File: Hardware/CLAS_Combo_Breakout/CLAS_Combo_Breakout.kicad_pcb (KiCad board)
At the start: 4 copper layers, 60 x 60 mm, 89 parts, among them J1 USB_C_Receptacle_USB2.0, J2 ZED, J3 NEO, J4 USB_C_Receptacle_USB2.0, J5 Conn_SMA, U1 USBLC6-2P6, U10 NT1191GEAE3S, U2 ZED-F9P, U3 NEO-D9C-00B, U4 USBLC6-2P6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

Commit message: 配線中
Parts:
- removed C9: 0.1u, Capacitor_SMD:C_0603_1608Metric
- moved C8 0.80 mm to (158.2, 130.1), turned to -90 degrees
- moved U6 0.76 mm to (157.9, 125.8)
- moved R4 0.57 mm to (153.1, 134.2)
- moved R18 0.57 mm to (155.9, 134.2)
- moved R3 0.36 mm to (153.1, 132.9)
- moved R27 0.36 mm to (155.9, 132.9)
- moved BT1 0.25 mm to (154.4, 129.6)
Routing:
- net /EXTINT_ZED: track 0.00 -> 25.3 mm, vias 0 -> 1
- net /TP: track 6.16 -> 29.6 mm, vias 0 -> 2
- net Net-(TP1-Pad1): track 0.00 -> 20.3 mm, vias 0 -> 2
- net /TX_RDY_: track 0.00 -> 15.0 mm, vias 0 -> 2
- net /RXD1_ZED: track 1.34 -> 14.7 mm
- net /VBUS_ZED: track 5.00 -> 11.0 mm, vias 2 -> 3

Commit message: 配線中
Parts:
- moved D7 3.30 mm to (158.2, 130.4), turned to 90 degrees
- moved R3 2.59 mm to (155.6, 133.4)
- moved R27 2.50 mm to (158.2, 133.9), turned to -90 degrees
- moved C8 1.91 mm to (158.2, 128.2), turned to 0 degrees
- moved R18 0.51 mm to (155.9, 134.7)
- moved R4 0.51 mm to (153.1, 134.7)
- moved BT1 0.25 mm to (154.4, 129.9)
- moved U6 0.25 mm to (157.9, 125.6)
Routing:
- net /V_BACKUP: track 0.00 -> 22.4 mm, vias 0 -> 2
- net /SDA: track 17.8 -> 32.9 mm, vias 0 -> 1
- net /SCL: track 12.7 -> 27.3 mm
- net /VBUS_ZED: track 11.0 -> 23.4 mm, vias 3 -> 4
- net /VBUS_NEO: track 29.3 -> 41.6 mm, vias 3 -> 4
- net +5V: track 0.00 -> 7.06 mm
- net /SCL_ZED_: track 0.00 -> 6.95 mm
- net /CC2_ZED: track 0.00 -> 5.75 mm
- net /SDA_ZED_: track 0.00 -> 4.21 mm
- net +3.3V: track 81.7 -> 85.9 mm
- net Net-(D7-Pad1): track 0.00 -> 1.78 mm

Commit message: I2C系統を配線
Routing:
- net /SDA: track 32.9 -> 82.6 mm
- net /SCL: track 27.3 -> 74.1 mm, vias 0 -> 1
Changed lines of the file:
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@@
   (via (at 151.562 101.316) (size 0.6) (drill 0.3) (layers "F.Cu" "B.Cu") (net 11))
   (arc (start 151.93 106.116) (mid 151.669785 106.008215) (end 151.562 105.748) (width 0.3) (layer "F.Cu") (net 11))
-  (segment (start 153.848 104.986) (end 151.562 104.986) (width 0.3) (layer "B.Cu") (net 11))
-  (segment (start 155.372 106.51) (end 153.848 104.986) (width 0.3) (layer "B.Cu") (net 11))
+  (segment (start 153.594 104.986) (end 151.562 104.986) (width 0.3) (layer "B.Cu") (net 11))
+  (segment (start 155.372 123.782) (end 155.372 109.304) (width 0.3) (layer "B.Cu") (net 11))
   (segment (start 154.356 96.604) (end 155.626 96.604) (width 0.3) (layer "B.Cu") (net 11))
+  (segment (start 154.864 108.796) (end 154.864 106.256) (width 0.3) (layer "B.Cu") (net 11))
   (segment (start 151.562 101.316) (end 151.562 99.398) (width 0.3) (layer "B.Cu") (net 11))
-  (segment (start 155.372 123.782) (end 155.372 106.51) (width 0.3) (layer "B.Cu") (net 11))
+  (segment (start 155.372 109.304) (end 154.864 108.796) (width 0.3) (layer "B.Cu") (net 11))
+  (segment (start 154.864 106.256) (end 153.594 104.986) (width 0.3) (layer "B.Cu") (net 11))
   (arc (start 151.562 99.398) (mid 152.380344 97.422344) (end 154.356 96.604) (width 0.3) (layer "B.Cu") (net 11))
   (segment (start 146.101 109.685) (end 142.829815 109.685) (width 0.35) (layer "F.Cu") (net 12))
@@
   (segment (start 150.546 145.88) (end 151.753 145.88) (width 0.2) (layer "F.Cu") (net 25))
   (segment (start 128.322 120.988) (end 126.866 120.988) (width 0.25) (layer "F.Cu") (net 27))
-  (segment (start 155.372 144.864) (end 154.356 145.88) (width 0.2) (layer "F.Cu") (net 28))
-  (segment (start 156.388 141.308) (end 155.372 142.324) (width 0.2) (layer "F.Cu") (net 28))
+  (segment (start 154.356 145.88) (end 153.403 145.88) (width 0.2) (layer "F.Cu") (net 28))
   (segment (start 149.53 92.794) (end 149.53 92.032) (width 0.2) (layer "F.Cu") (net 28))
-  (segment (start 155.88 136.482) (end 156.388 136.99) (width 0.2) (layer "F.Cu") (net 28))
-  (segment (start 154.356 145.88) (end 153.403 145.88) (width 0.2) (layer "F.Cu") (net 28))
-  (segment (start 156.405745 133.543255) (end 156.134 133.815) (width 0.2) (layer "F.Cu") (net 28))
-  (segment (start 156.388 136.99) (end 156.388 141.308) (width 0.2) (layer "F.Cu") (net 28))
+  (segment (start 155.88 134.42821) (end 155.88 135.466) (width 0.2) (layer "F.Cu") (net 28))
   (segment (start 153.34 92.032) (end 152.42921 91.12121) (width 0.2) (layer "F.Cu") (net 28))
   (segment (start 153.34 147.912) (end 153.34 145.943) (width 0.2) (layer "F.Cu") (net 28))
   (segment (start 151.562 90.762) (end 150.8 90.762) (width 0.2) (layer "F.Cu") (net 28))
+  (segment (start 155.372 144.864) (end 154.356 145.88) (width 0.2) (layer "F.Cu") (net 28))
+  (segment (start 155.88 135.466) (end 155.88 136.736) (width 0.2) (layer "F.Cu") (net 28))
+  (segment (start 156.388 137.244) (end 156.388 141.308) (width 0.2) (layer "F.Cu") (net 28))
   (segment (start 155.372 142.324) (end 155.372 144.864) (width 0.2) (layer "F.Cu") (net 28))
   (segment (start 145.148 93.81) (end 148.514 93.81) (width 0.2) (layer "F.Cu") (net 28))
-  (segment (start 155.88 134.42821) (end 155.88 136.482) (width 0.2) (layer "F.Cu") (net 28))
+  (segment (start 156.388 141.308) (end 155.372 142.324) (width 0.2) (layer "F.Cu") (net 28))
+  (segment (start 155.88 136.736) (end 156.388 137.244) (width 0.2) (layer "F.Cu") (net 28))
+  (segment (start 156.134 133.815) (end 156.405745 133.543255) (width 0.2) (layer "F.Cu") (net 28))
+  (via (at 155.88 135.466) (size 0.6) (drill 0.3) (layers "F.Cu" "B.Cu") (net 28))
   (arc (start 149.53 92.032) (mid 149.901974 91.133974) (end 150.8 90.762) (width 0.2) (layer "F.Cu") (net 28))
+  (arc (start 156.405745 133.543255) (mid 156.439239 133.493128) (end 156.451 133.434) (width 0.2) (layer "F.Cu") (net 28))
   (arc (start 148.514 93.81) (mid 149.23242 93.51242) (end 149.53 92.794) (width 0.2) (layer "F.Cu") (net 28))
   (arc (start 152.42921 91.12121) (mid 152.031331 90.855356) (end 151.562 90.762) (width 0.2) (layer "F.Cu") (net 28))
-  (arc (start 156.451 133.434) (mid 156.439239 133.493128) (end 156.405745 133.543255) (width 0.2) (layer "F.Cu") (net 28))
+  (arc (start 155.88 134.42821) (mid 155.946012 134.096343) (end 156.134 133.815) (width 0.2) (layer "F.Cu") (net 28))
   (arc (start 153.34 145.943) (mid 153.358452 145.898452) (end 153.403 145.88) (width 0.2) (layer "F.Cu") (net 28))
-  (arc (start 156.134 133.815) (mid 155.946012 134.096343) (end 155.88 134.42821) (width 0.2) (layer "F.Cu") (net 28))
+  (segment (start 158.674 108.542) (end 158.674 98.636) (width 0.2) (layer "B.Cu") (net 28))
+  (segment (start 153.34 92.94279) (end 153.34 92.032) (width 0.2) (layer "B.Cu") (net 28))
+  (segment (start 157.404 133.942) (end 157.404 121.496) (width 0.2) (layer "B.Cu") (net 28))
+  (segment (start 157.404 121.496) (end 158.42 120.48) (width 0.2) (layer "B.Cu") (net 28))
+  (segment (start 155.88 135.466) (end 157.404 133.942) (width 0.2) (layer "B.Cu") (net 28))
+  (segment (start 158.42 108.796) (end 158.674 108.542) (width 0.2) (layer "B.Cu") (net 28))
+  (segment (start 158.674 98.636) (end 153.594 93.556) (width 0.2) (layer "B.Cu") (net 28))
+  (segment (start 158.42 120.48) (end 158.42 108.796) (width 0.2) (layer "B.Cu") (net 28))
+  (arc (start 153.594 93.556) (mid 153.406013 93.274656) (end 153.34 92.94279) (width 0.2) (layer "B.Cu") (net 28))
   (segment (start 154.61 136.736) (end 154.61 135.466) (width 0.2) (layer "F.Cu") (net 29))
   (segment (start 145.657 145.88) (end 144.853759 146.683241) (width 0.2) (layer "F.Cu") (net 29))
@@
   (arc (start 144.45 147.912) (mid 144.821974 148.810026) (end 145.72 149.182) (width 0.2) (layer "F.Cu") (net 29))
   (arc (start 146.736 95.08) (mid 146.970665 95.033322) (end 147.169605 94.900395) (width 0.2) (layer "F.Cu") (net 29))
+  (segment (start 154.102 102.446) (end 156.134 104.478) (width 0.2) (layer "B.Cu") (net 29))
   (segment (start 150.8 144.61) (end 150.8 147.912) (width 0.2) (layer "B.Cu") (net 29))
+  (segment (start 150.8 92.032) (end 150.8 101.684) (width 0.2) (layer "B.Cu") (net 29))
+  (segment (start 156.388 125.56) (end 154.61 127.338) (width 0.2) (layer "B.Cu") (net 29))
+  (segment (start 156.134 104.478) (end 156.134 108.542) (width 0.2) (layer "B.Cu") (net 29))
   (segment (start 154.61 140.8) (end 150.8 144.61) (width 0.2) (layer "B.Cu") (net 29))
   (segment (start 154.61 136.736) (end 154.61 140.8) (width 0.2) (layer "B.Cu") (net 29))
+  (segment (start 150.8 101.684) (end 151.562 102.446) (width 0.2) (layer "B.Cu") (net 29))
+  (segment (start 156.134 108.542) (end 156.896 109.304) (width 0.2) (layer "B.Cu") (net 29))
+  (segment (start 156.896 109.304) (end 156.896 119.972) (width 0.2) (layer "B.Cu") (net 29))
+  (segment (start 156.896 119.972) (end 156.388 120.48) (width 0.2) (layer "B.Cu") (net 29))
+  (segment (start 154.61 127.338) (end 154.61 136.736) (width 0.2) (layer "B.Cu") (net 29))
+  (segment (start 156.388 120.48) (end 156.388 125.56) (width 0.2) (layer "B.Cu") (net 29))
+  (segment (start 151.562 102.446) (end 154.102 102.446) (width 0.2) (layer "B.Cu") (net 29))
   (segment (start 150.546 142.197) (end 150.546 142.769) (width 0.2) (layer "F.Cu") (net 30))
   (segment (start 152.655 141.542) (end 151.201 141.542) (width 0.2) (layer "F.Cu") (net 30))

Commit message: 配線中
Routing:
- net /RESET: track 20.1 -> 62.8 mm, vias 1 -> 2
- net +3.3V: track 85.9 -> 115.5 mm, vias 4 -> 7
- net /VBUS_ZED: track 23.4 -> 25.0 mm
- net +5V: track 7.06 -> 8.58 mm
- net /VBUS_NEO: track 41.5 -> 40.5 mm
- net Net-(D9-Pad3): track 11.7 -> 12.7 mm

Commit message: 配線中、残り3V3
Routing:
- net /EXTANT_DETECT: track 3.52 -> 33.2 mm, vias 0 -> 1
- net Net-(D9-Pad3): track 12.7 -> 13.6 mm
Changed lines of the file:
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@@
   (segment (start 143.434 143.34) (end 142.926 143.848) (width 0.25) (layer "F.Cu") (net 6))
   (segment (start 144.196 142.832) (end 143.955 142.832) (width 0.25) (layer "F.Cu") (net 6))
+  (segment (start 134.036 104.745) (end 140.760999 104.745) (width 0.25) (layer "F.Cu") (net 6))
   (segment (start 128.322 120.488) (end 128.322 119.59) (width 0.25) (layer "F.Cu") (net 6))
   (segment (start 146.482 145.626) (end 146.482 146.134) (width 0.25) (layer "F.Cu") (net 6))
@@
   (segment (start 158.166 129.436) (end 155.245 129.436) (width 0.25) (layer "F.Cu") (net 6))
   (segment (start 158.862 126.6975) (end 158.4255 126.6975) (width 0.25) (layer "F.Cu") (net 6))
-  (segment (start 134.036 104.745) (end 139.878 104.745) (width 0.25) (layer "F.Cu") (net 6))
   (via (at 138.354 94.572) (size 0.6) (drill 0.3) (layers "F.Cu" "B.Cu") (net 6))
   (via (at 142.779999 106.764) (size 0.6) (drill 0.3) (layers "F.Cu" "B.Cu") (net 6))
   (via (at 144.323 137.371) (size 0.6) (drill 0.3) (layers "F.Cu" "B.Cu") (net 6))
-  (via (at 139.878 104.745) (size 0.6) (drill 0.3) (layers "F.Cu" "B.Cu") (net 6))
+  (via (at 140.760999 104.745) (size 0.6) (drill 0.3) (layers "F.Cu" "B.Cu") (net 6))
   (via (at 130.988 118.956) (size 0.6) (drill 0.3) (layers "F.Cu" "B.Cu") (net 6))
   (via (at 155.245 129.436) (size 0.6) (drill 0.3) (layers "F.Cu" "B.Cu") (net 6))
@@
   (arc (start 148.26 147.912) (mid 148.025335 147.865322) (end 147.826395 147.732395) (width 0.25) (layer "F.Cu") (net 6))
   (segment (start 148.26 92.032) (end 147.336446 92.955554) (width 0.25) (layer "B.Cu") (net 6))
-  (segment (start 140.760999 104.745) (end 142.779999 106.764) (width 0.25) (layer "B.Cu") (net 6))
   (segment (start 155.245 129.436) (end 152.258 129.436) (width 0.25) (layer "B.Cu") (net 6))
   (segment (start 143.561 107.545001) (end 143.561 114.45) (width 0.25) (layer "B.Cu") (net 6))
+  (segment (start 140.760999 104.745) (end 142.779999 106.764) (width 0.25) (layer "B.Cu") (net 6))
   (segment (start 142.779999 106.764) (end 143.561 107.545001) (width 0.25) (layer "B.Cu") (net 6))
   (segment (start 152.258 129.436) (end 144.323 137.371) (width 0.25) (layer "B.Cu") (net 6))
-  (segment (start 139.878 104.745) (end 140.760999 104.745) (width 0.25) (layer "B.Cu") (net 6))
   (segment (start 143.434 94.572) (end 138.354 94.572) (width 0.25) (layer "B.Cu") (net 6))
   (arc (start 147.336446 92.955554) (mid 145.545988 94.151899) (end 143.434 94.572) (width 0.25) (layer "B.Cu") (net 6))
@@
   (segment (start 143.497 118.702) (end 143.497 117.432) (width 0.35) (layer "F.Cu") (net 39))
   (segment (start 144.641 117.432) (end 144.641 116.4195) (width 0.35) (layer "F.Cu") (net 39))
+  (segment (start 144.5715 116.35) (end 143.561 116.35) (width 0.6) (layer "F.Cu") (net 39))
+  (via (at 143.561 116.35) (size 0.6) (drill 0.3) (layers "F.Cu" "B.Cu") (net 39))
+  (segment (start 133.02 98.89) (end 141.275 107.145) (width 0.2) (layer "B.Cu") (net 39))
+  (segment (start 141.275 114.064) (end 143.561 116.35) (width 0.2) (layer "B.Cu") (net 39))
+  (segment (start 141.275 107.145) (end 141.275 114.064) (width 0.2) (layer "B.Cu") (net 39))
+  (segment (start 133.02 92.032) (end 133.02 98.89) (width 0.2) (layer "B.Cu") (net 39))
   (segment (start 128.448 135.82521) (end 127.432 136.84121) (width 0.2) (layer "F.Cu") (net 40))
   (segment (start 130.035 142.832) (end 129.146 141.943) (width 0.2) (layer "F.Cu") (net 40))
@@
   (arc (start 146.101 112.352) (mid 146.24162 112.562453) (end 146.291 112.8107) (width 0.35) (layer "F.Cu") (net 100))
   (arc (start 145.8955 111.85588) (mid 145.948908 112.124378) (end 146.101 112.352) (width 0.35) (layer "F.Cu") (net 100))
-  (segment (start 144.958 116.162) (end 140.701405 116.162) (width 0.35) (layer "B.Cu") (net 100))
-  (segment (start 145.593 113.368) (end 145.593 115.527) (width 0.35) (layer "B.Cu") (net 100))
+  (segment (start 142.799 117.051) (end 141.91 116.162) (width 0.35) (layer "B.Cu") (net 100))
+  (segment (start 141.91 116.162) (end 140.701405 116.162) (width 0.35) (layer "B.Cu") (net 100))
+  (segment (start 145.593 113.368) (end 145.593 115.781) (width 0.35) (layer "B.Cu") (net 100))
+  (segment (start 145.593 115.781) (end 144.323 117.051) (width 0.35) (layer "B.Cu") (net 100))
+  (segment (start 144.323 117.051) (end 142.799 117.051) (width 0.35) (layer "B.Cu") (net 100))
   (segment (start 140.005 116.858405) (end 140.005 116.924) (width 0.35) (layer "B.Cu") (net 100))
-  (arc (start 144.958 116.162) (mid 145.407013 115.976013) (end 145.593 115.527) (width 0.35) (layer "B.Cu") (net 100))
   (arc (start 140.701405 116.162) (mid 140.208972 116.365972) (end 140.005 116.858405) (width 0.35) (layer "B.Cu") (net 100))
   (segment (start 145.657 142.2747) (end 145.657 142.832) (width 0.2) (layer "F.Cu") (net 101))

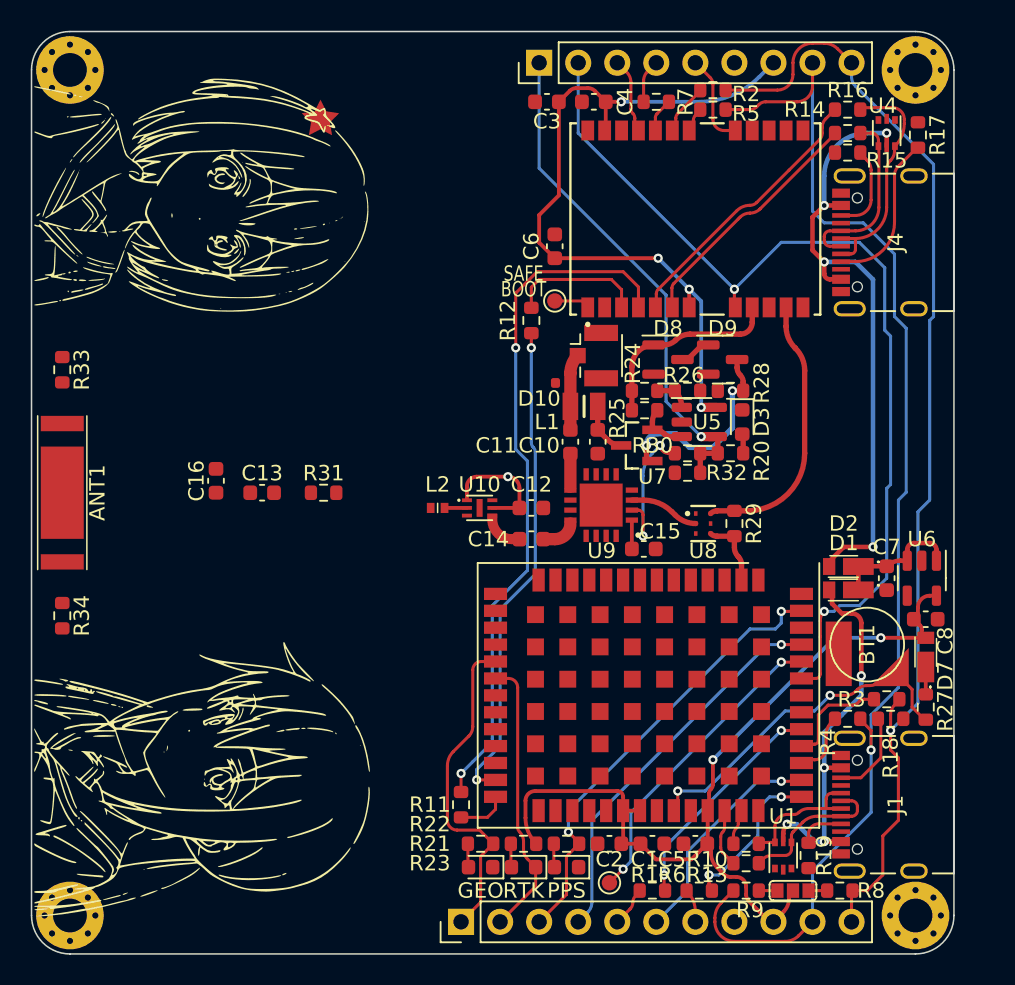
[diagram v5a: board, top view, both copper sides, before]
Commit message: 3V3パスを配線、ZED周辺のパスを改善したい
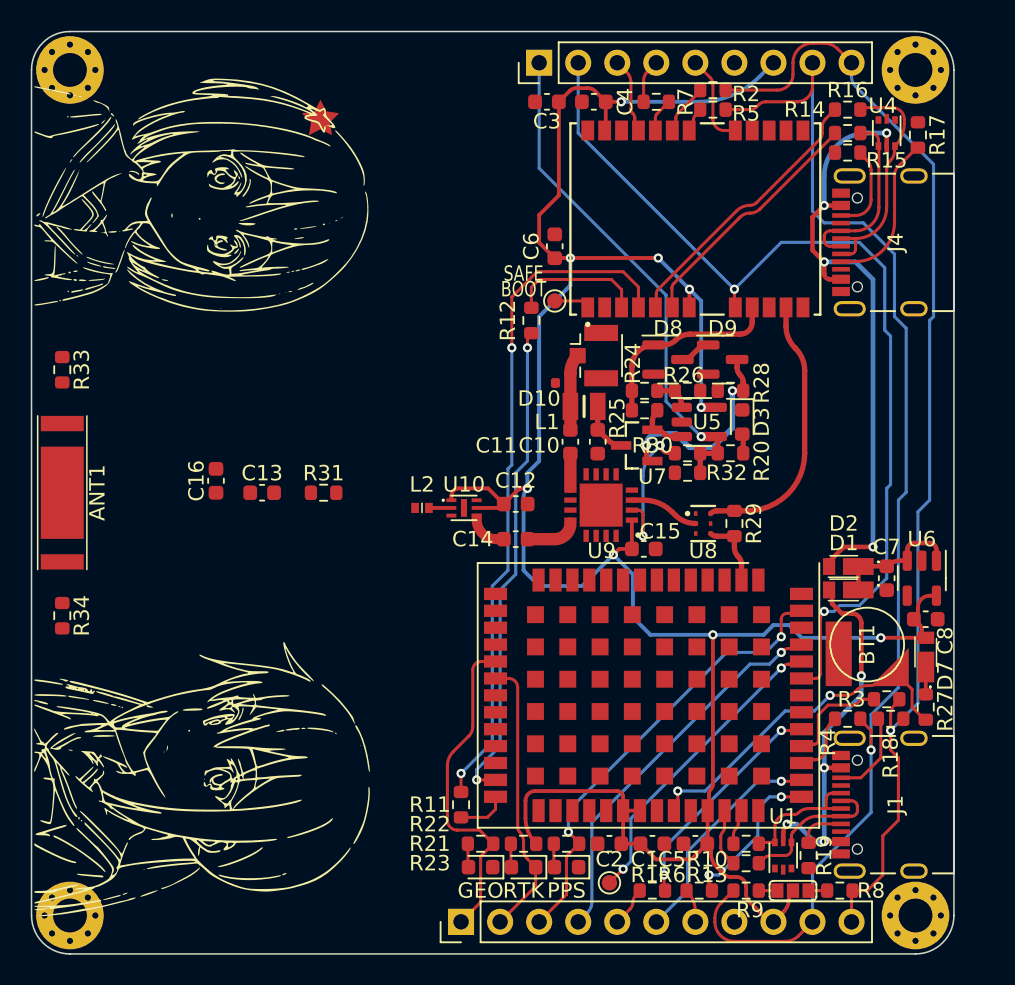
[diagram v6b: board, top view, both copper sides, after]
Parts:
- moved C12 1.05 mm to (131.5, 120.7)
- moved C14 1.02 mm to (131.5, 123.0)
- moved L2 1.02 mm to (125.4, 121.0)
- moved U10 1.02 mm to (128.1, 121.0)
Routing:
- net +3.3V: track 115.5 -> 161.3 mm, vias 7 -> 9
- net Net-(C14-Pad1): track 2.30 -> 3.32 mm
- net Net-(R11-Pad2): track 44.9 -> 44.2 mm

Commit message: 配線パスを改善
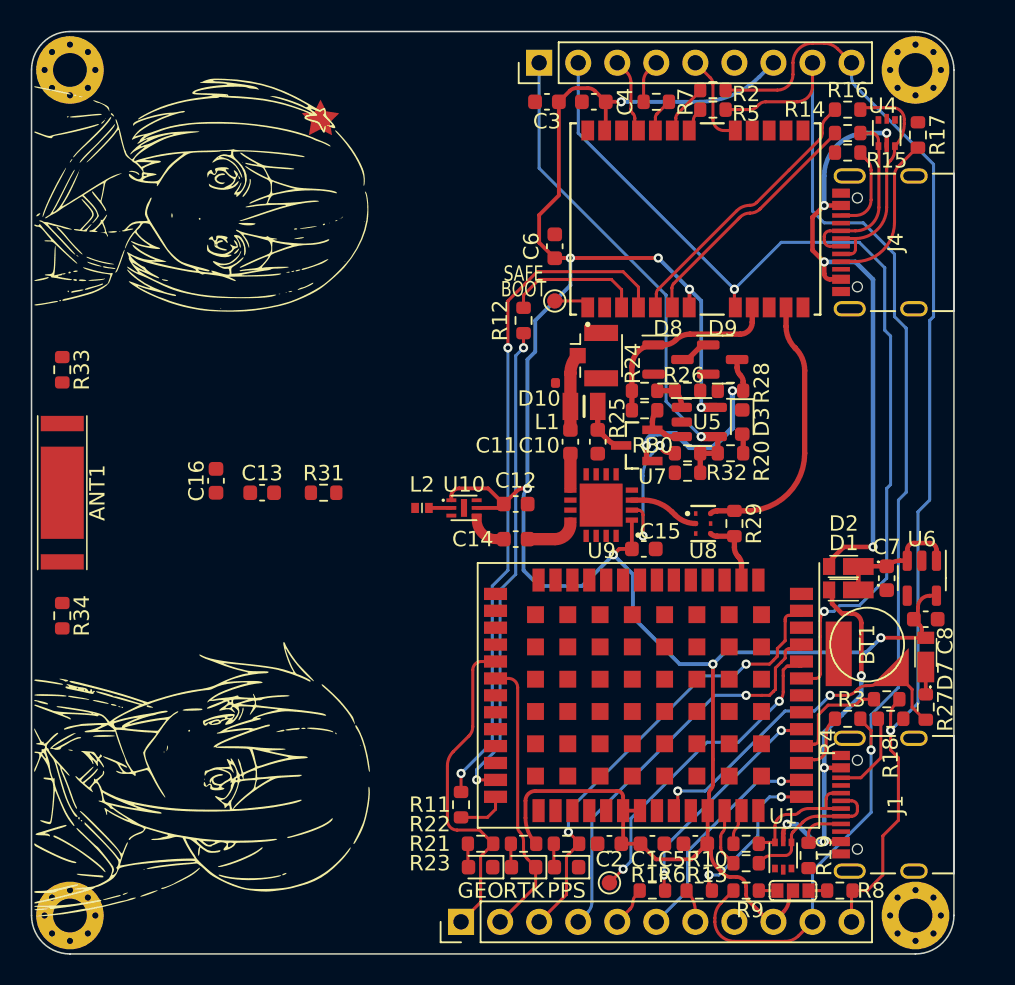
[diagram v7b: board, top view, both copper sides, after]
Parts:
- moved R12 0.51 mm to (132.0, 108.8)
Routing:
- net /EXTINT_ZED: track 25.3 -> 26.6 mm
- net Net-(TP1-Pad1): track 20.2 -> 21.3 mm
- net +3.3V: track 161.3 -> 160.3 mm
- net /TP: track 29.9 -> 30.5 mm

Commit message: 配線を迂回中
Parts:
- moved R12 23.9 mm to (155.9, 109.8), turned to 0 degrees
- moved L2 0.51 mm to (124.9, 121.0)
- moved U10 0.51 mm to (127.6, 121.0)
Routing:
- net Net-(R11-Pad2): track 44.2 -> 25.8 mm, vias 2 -> 1
- net Net-(R12-Pad1): track 31.5 -> 20.7 mm, vias 2 -> 1
- net +3.3V: track 160.3 -> 169.3 mm, vias 9 -> 10
- net /RESET: track 62.8 -> 54.9 mm
- net Net-(R12-Pad2): track 9.05 -> 3.79 mm
- net /RTK: track 18.3 -> 21.9 mm
- net /SDA: track 82.6 -> 84.0 mm
- net /ANT_NEO: track 17.9 -> 17.0 mm
- net /VBUS_NEO: track 40.5 -> 39.8 mm
- net Net-(C14-Pad2): track 2.44 -> 2.95 mm
